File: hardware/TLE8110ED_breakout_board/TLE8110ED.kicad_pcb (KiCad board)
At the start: 2 copper layers, 59.1 x 40.6 mm, 7 parts, among them J1 Conn_01x18, J2 Screw_Terminal_01x16, U1 TLE8110ED

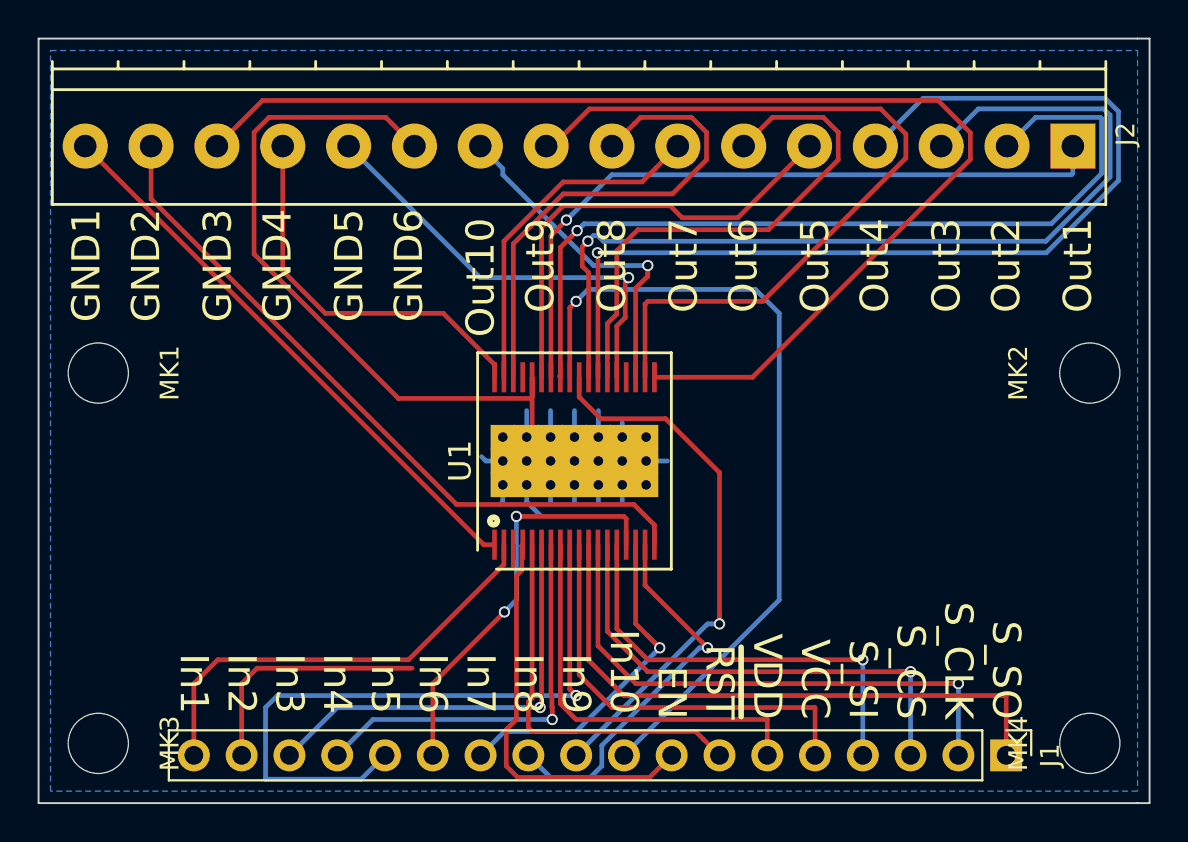
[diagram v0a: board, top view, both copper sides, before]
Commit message: Implemented a few helpful suggestions. Improved silscreen and titel block.
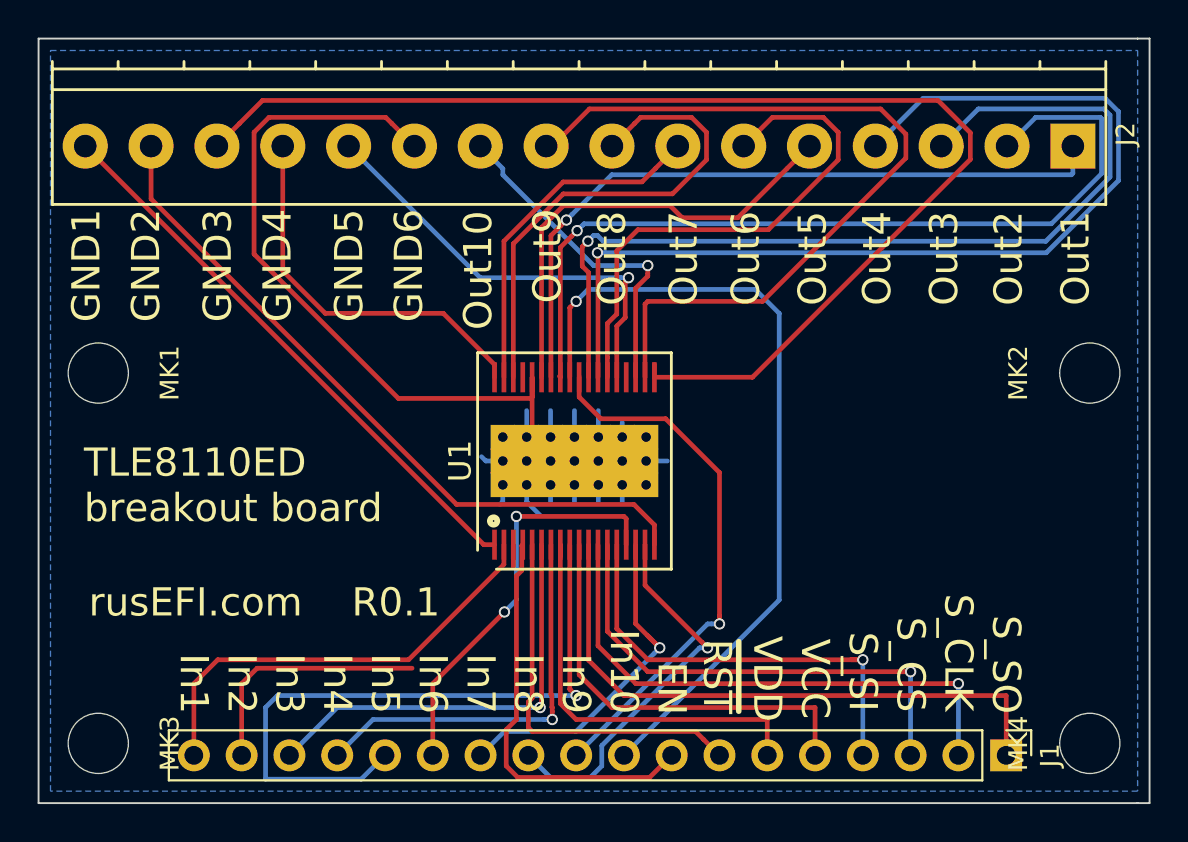
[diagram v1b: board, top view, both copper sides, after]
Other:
- board text added: "TLE8110ED breakout board"
- board text added: "rusEFI.com R0.1"
